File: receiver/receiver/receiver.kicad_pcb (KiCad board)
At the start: 2 copper layers, 2 parts

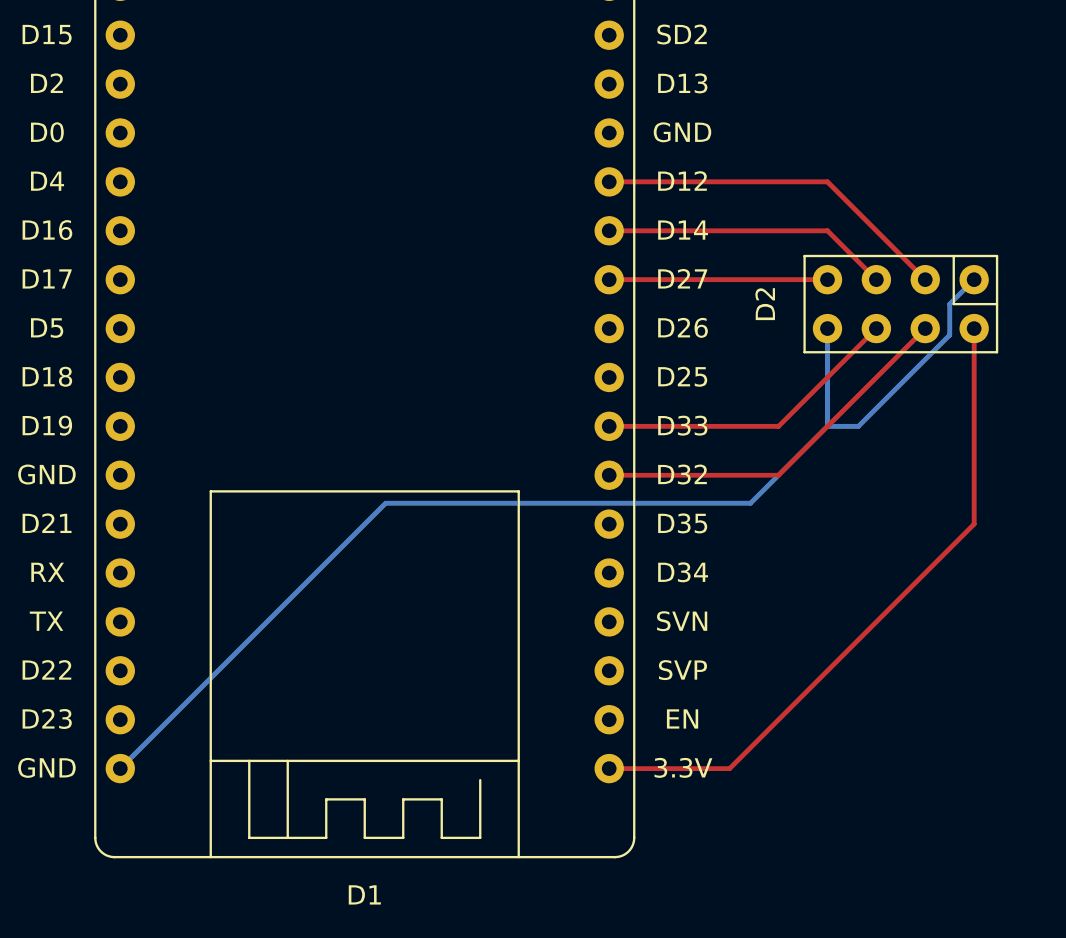
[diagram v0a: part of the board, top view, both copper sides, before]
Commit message: add 100mF capacitor
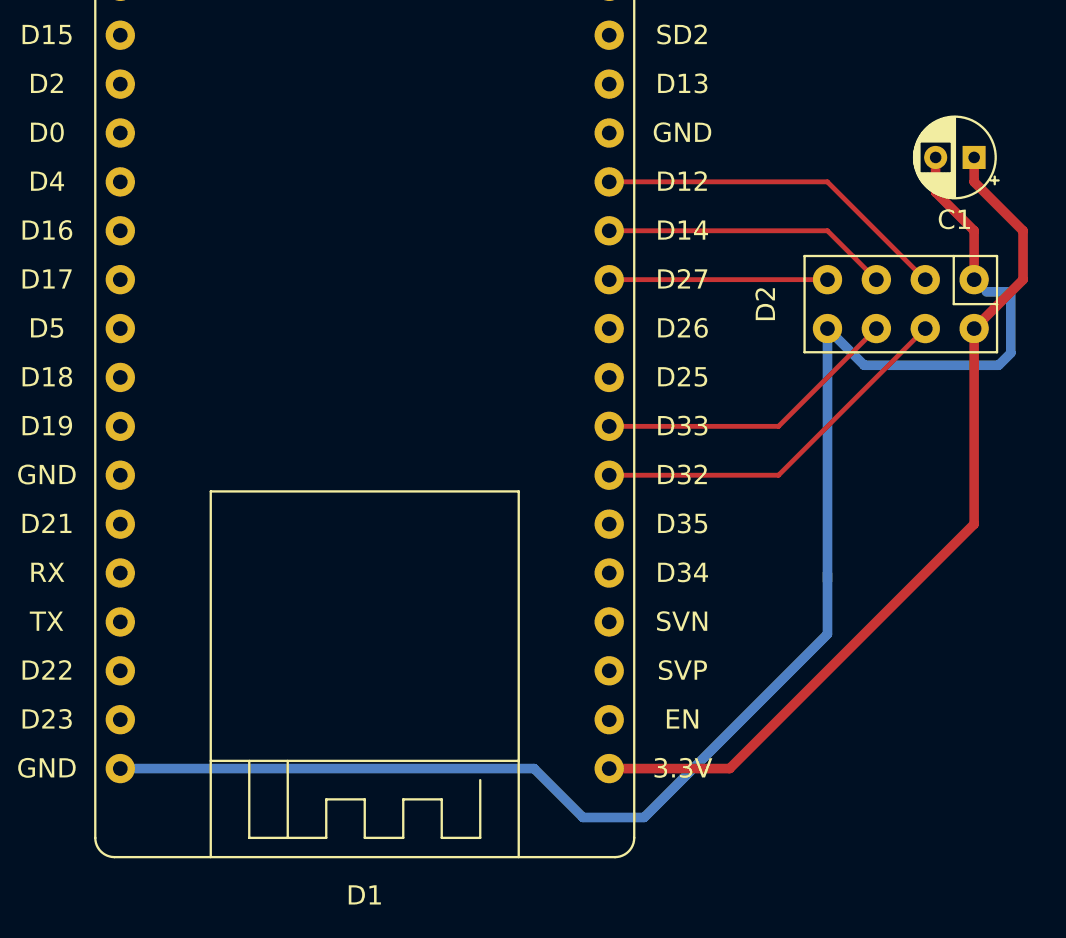
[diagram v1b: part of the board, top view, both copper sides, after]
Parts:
- added C1: 100microF, Capacitor_THT:CP_Radial_D4.0mm_P2.00mm, F.Cu at (161.3, 71.1)
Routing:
- net GND1: track 60.9 -> 81.1 mm
- net +3V3: track 34.4 -> 45.4 mm

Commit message: add pins
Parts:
- added C2: 470microF, Capacitor_THT:CP_Radial_D8.0mm_P3.50mm, F.Cu at (155.6, 57.1)
- added C3: 0.1microF, Capacitor_THT:C_Disc_D3.0mm_W2.0mm_P2.50mm, F.Cu at (74.3, 113.7)
- added C4: 470microF, Capacitor_THT:CP_Radial_D8.0mm_P3.50mm, F.Cu at (73.7, 107.3)
- added C5: 0.1microF, Capacitor_THT:C_Disc_D3.0mm_W2.0mm_P2.50mm, F.Cu at (165.1, 56.5)
- added C6: 0.1microF, Capacitor_THT:C_Disc_D3.0mm_W2.0mm_P2.50mm, F.Cu at (161.3, 66.0)
- added D3: servo_connector, Connector_PinHeader_2.54mm:PinHeader_1x03_P2.54mm_Vertical, F.Cu at (74.3, 92.7)
- added D4: servo_connector, Connector_PinHeader_2.54mm:PinHeader_1x03_P2.54mm_Vertical, F.Cu at (74.3, 95.2)
- added D5: servo_connector, Connector_PinHeader_2.54mm:PinHeader_1x03_P2.54mm_Vertical, F.Cu at (74.3, 97.8)
- added D6: servo_connector, Connector_PinHeader_2.54mm:PinHeader_1x03_P2.54mm_Vertical, F.Cu at (74.3, 100.3)
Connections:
- D1 pad 10: Net-(D1-Pad10) -> /D5
- D1 pad 14: Net-(D1-Pad14) -> /D21
- D1 pad 17: Net-(D1-Pad17) -> /D22
- D1 pad 18: Net-(D1-Pad18) -> /D23
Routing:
- net GND: track 0.00 -> 158.6 mm
- net +7.5V: track 0.00 -> 140.0 mm
- net /D5: track 0.00 -> 42.8 mm
- net /D21: track 0.00 -> 39.7 mm
- net /D23: track 0.00 -> 37.6 mm
- net /D22: track 0.00 -> 37.6 mm
- net GND1: track 81.1 -> 86.4 mm
- net +3V3: track 45.4 -> 50.5 mm

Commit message: LM2596
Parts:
- added D10: cleat_2pin, common:cleat_2pin, F.Cu at (181.6, 52.1)
- added D11: LM2596, common:LM2596, F.Cu at (176.5, 81.3)
- added D7: 3.3V, common:3.3V-converter, F.Cu at (96.5, 59.7)
- added D8: 5.0V, common:5.0V-converter, F.Cu at (106.7, 59.7)
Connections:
- C1 pad 2: GND1 -> GND2
- C2 pad 1: GND -> GND1
- C3 pad 1: GND -> GND1
- C4 pad 1: GND -> GND1
- C5 pad 1: GND -> GND1
- C6 pad 2: GND1 -> GND2
- D1 pad 19: GND1 -> GND2
- D1 pad 33: GND -> GND1
- D2 pad 1: GND1 -> GND2
- D2 pad 5: GND1 -> GND2
- D3 pad 1: GND -> GND1
- D4 pad 1: GND -> GND1
- D5 pad 1: GND -> GND1
- D6 pad 1: GND -> GND1
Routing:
- net GND1: track 86.4 -> 236.0 mm
- net GND: track 158.6 -> 15.1 mm
- net GND2: track 0.00 -> 86.4 mm
- net +7.5V: track 140.0 -> 207.0 mm
- net +12V: track 0.00 -> 9.89 mm
